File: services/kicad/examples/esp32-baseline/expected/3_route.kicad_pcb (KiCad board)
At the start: 2 copper layers, 93.1 x 69.8 mm, 20 parts, among them J1 5V, U1 ESP32-WROOM-32, U2 AMS1117-3.3

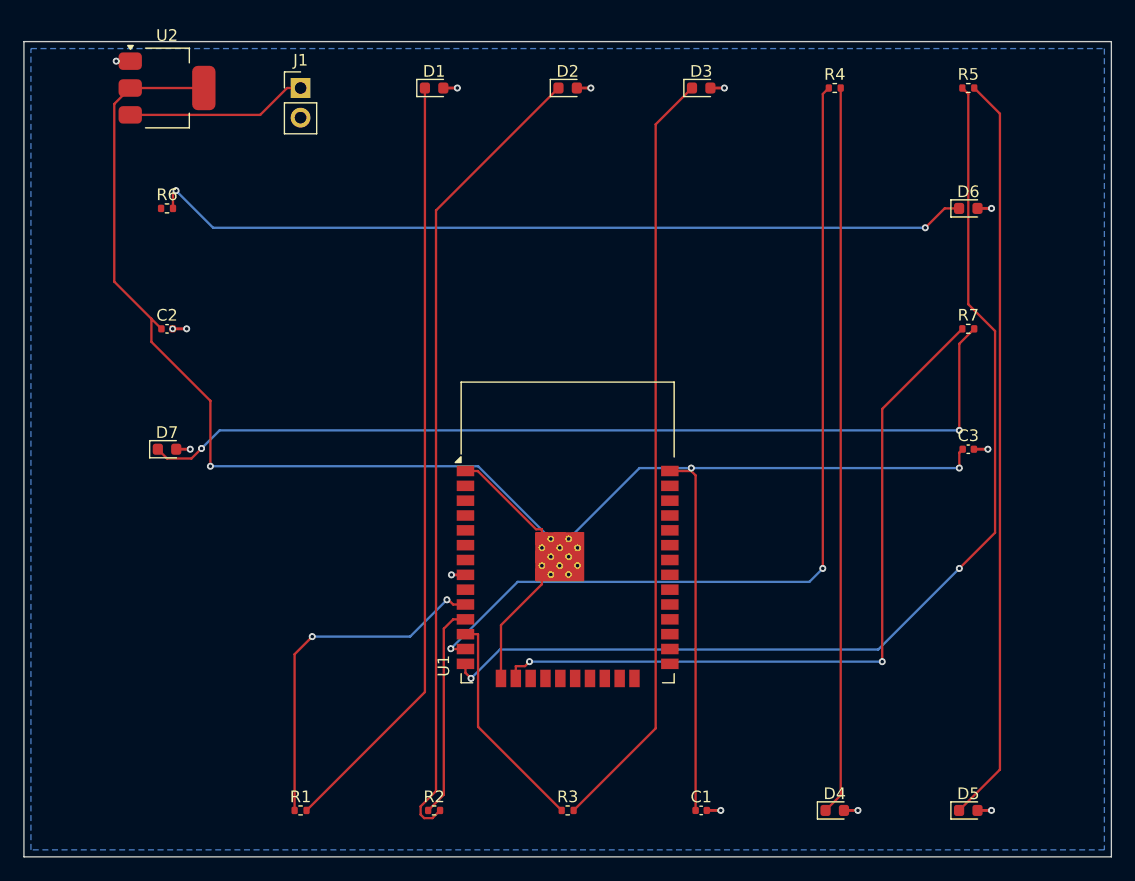
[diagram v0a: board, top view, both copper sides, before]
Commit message: test(examples): references stm32-*/esp32 -- 3_route.kicad_pcb et mesures-routage.json alignes sur les boards livres
Co-Authored-By: Claude Fable 5.1 <noreply@anthropic.com>
Claude-Session: https://claude.ai/code/session_01TnMqm4La2CxQHHB5K8aSSV
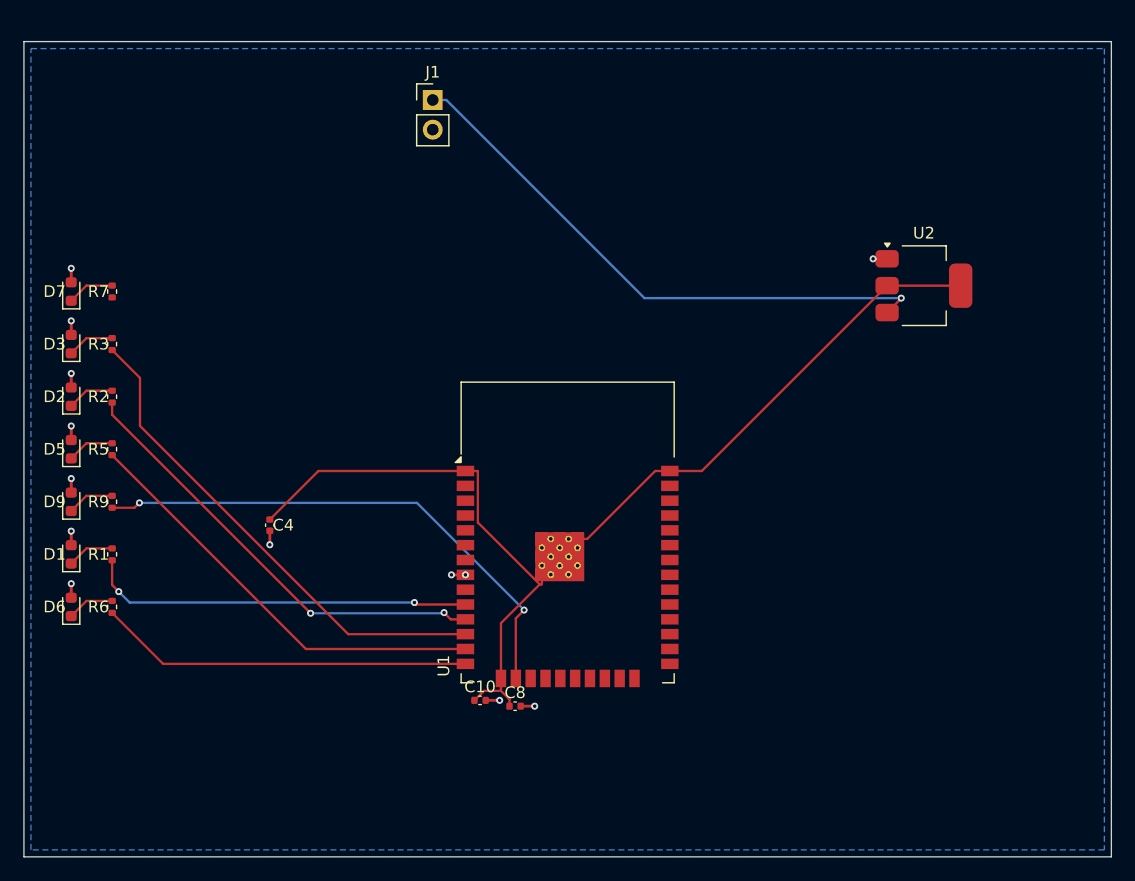
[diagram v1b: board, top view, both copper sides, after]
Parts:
- removed C1, C2, C3: 100nF, C_0402_1005Metric
- removed D4: LED, LED_0603_1608Metric
- removed R4: 330, R_0402_1005Metric
- added C10: 100nF, C_0402_1005Metric, F.Cu at (141.0, 126.5)
- added C4: 100nF, C_0402_1005Metric, F.Cu at (123.0, 111.5)
- added C8: 100nF, C_0402_1005Metric, F.Cu at (144.0, 127.0)
- added D9: LED, LED_0603_1608Metric, F.Cu at (106.0, 109.5)
- added R9: 330, R_0402_1005Metric, F.Cu at (109.5, 109.5)
- moved D6 84.0 mm to (106.0, 118.5), turned to 90 degrees
- moved D5 82.8 mm to (106.0, 105.0), turned to 90 degrees
- moved R5 79.6 mm to (109.5, 105.0), turned to 90 degrees
- moved R7 73.4 mm to (109.5, 91.5), turned to 90 degrees
- moved U2 67.0 mm to (179.0, 91.0)
- moved D3 58.2 mm to (106.0, 96.0), turned to 90 degrees
- moved R3 55.8 mm to (109.5, 96.0), turned to 90 degrees
- moved D1 50.6 mm to (106.0, 114.0), turned to 90 degrees
- moved D2 50.0 mm to (106.0, 100.5), turned to 90 degrees
- moved R2 44.9 mm to (109.5, 100.5), turned to 90 degrees
- moved R6 34.4 mm to (109.5, 118.5), turned to 90 degrees
- moved R1 27.2 mm to (109.5, 114.0), turned to 90 degrees
- moved D7 15.8 mm to (106.0, 91.5), turned to 90 degrees
- moved J1 11.4 mm to (136.9, 75.1)
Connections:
- D5 pad 1: LED6 -> LED5
- D6 pad 1: LED7 -> LED6
- D7 pad 1: LED9 -> LED7
- R5 pad 1: GPIO6 -> GPIO5
- R5 pad 2: LED6 -> LED5
- R6 pad 1: GPIO7 -> GPIO6
- R6 pad 2: LED7 -> LED6
- R7 pad 1: GPIO9 -> GPIO7
- R7 pad 2: LED9 -> LED7
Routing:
- net LED9: track 79.2 -> 4.04 mm, vias 2 -> 0
- net +3V3: track 183.4 -> 109.0 mm, vias 3 -> 0
- net LED7: track 70.7 -> 4.04 mm, vias 2 -> 0
- net LED2: track 69.2 -> 4.04 mm
- net LED1: track 66.0 -> 4.04 mm
- net LED3: track 66.0 -> 4.04 mm
- net LED6: track 64.2 -> 4.04 mm
- net GPIO6: track 90.7 -> 32.1 mm, vias 2 -> 0
- net LED5: track 62.4 -> 4.04 mm
- net GPIO5: track 77.3 -> 37.1 mm, vias 2 -> 0
- net VIN: track 15.5 -> 48.9 mm, vias 0 -> 1
- net GPIO3: track 19.1 -> 42.7 mm
- net GPIO2: track 18.3 -> 38.6 mm, vias 0 -> 2
- net GPIO9: track 63.9 -> 45.4 mm
- net GPIO1: track 30.1 -> 33.1 mm
